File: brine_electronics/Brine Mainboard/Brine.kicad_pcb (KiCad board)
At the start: 2 copper layers, 30.4 x 42.6 mm, 29 parts, among them J1 BATT, J2 BATT_CRG_GND, J3 BATT_CRG_BATT, J4 BATT_CRG_BATT, J5 BATT_CRG_GND, Q1 AO3407A, U1 XIAO-ESP32-S3-SMD, U2 VL53L1CXV0FY1, U3 LTC2954, U4 74AHCT1G125

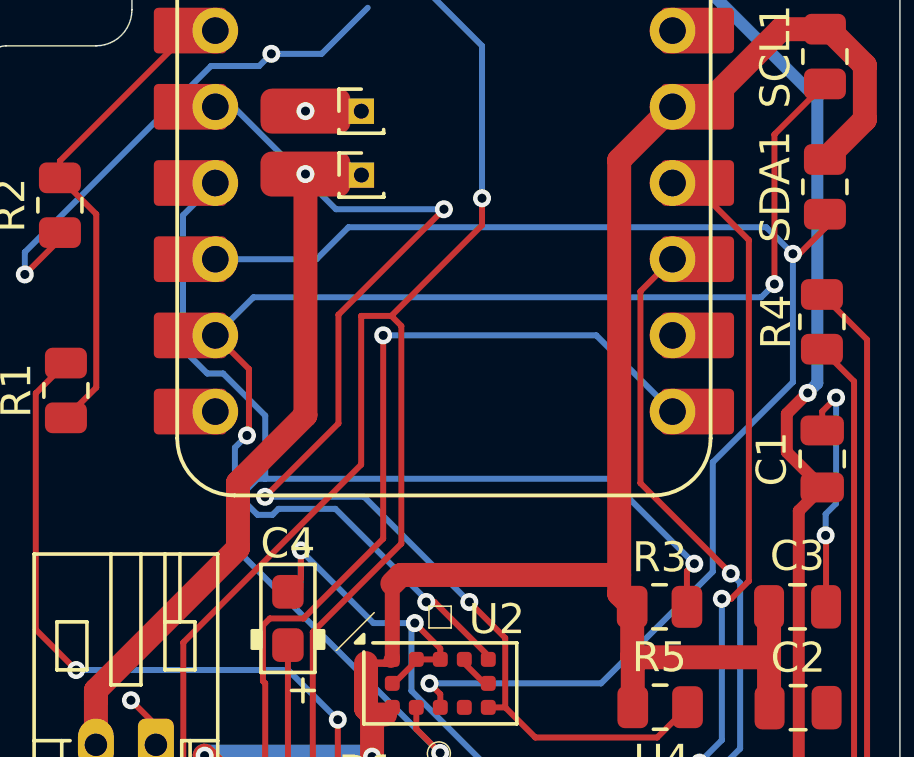
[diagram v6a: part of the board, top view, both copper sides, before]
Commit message: Updated GPIO button wiring ⚡
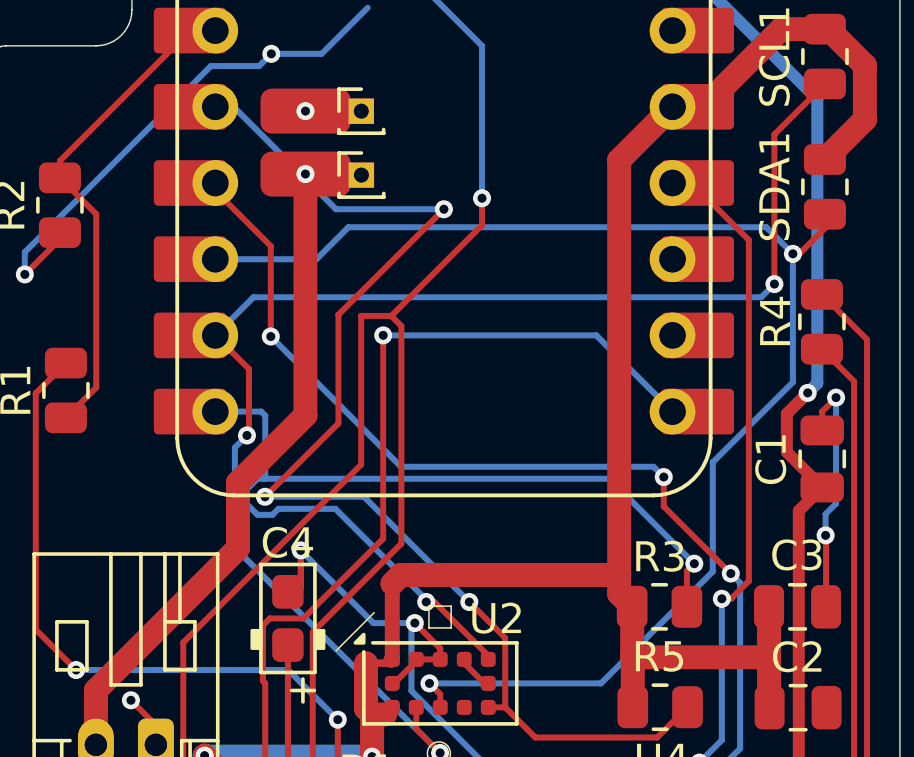
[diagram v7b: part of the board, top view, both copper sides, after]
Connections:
- U1 pad 10: /Button/BUTTON -> unconnected-(U1-GPIO9_D9_MISO-Pad10)
- U1 pad 4: /Distance Sensor/XSHUT -> /Button/BUTTON
- U1 pad 7: unconnected-(U1-GPIO21_D6_TX-Pad7)_1 -> /Distance Sensor/XSHUT
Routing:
- net /Button/BUTTON: track 60.5 -> 73.4 mm, vias 3 -> 5
- net /Distance Sensor/XSHUT: track 41.3 -> 32.6 mm
- net unconnected-(U1-GPIO9_D9_MISO-Pad10): track 0.00 -> 0.83 mm
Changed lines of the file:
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@@
 			(layers "F.Cu" "F.Mask")
 			(roundrect_rratio 0.1)
-			(net "/Distance Sensor/XSHUT")
+			(net "/Button/BUTTON")
 			(pinfunction "GPIO5_A3_D3_4")
 			(pintype "passive")
@@
 			(layers "*.Cu" "*.Mask")
 			(remove_unused_layers no)
-			(net "/Distance Sensor/XSHUT")
+			(net "/Button/BUTTON")
 			(pinfunction "GPIO5_A3_D3_4")
 			(pintype "passive")
@@
 			(layers "F.Cu" "F.Mask")
 			(roundrect_rratio 0.1)
-			(net "unconnected-(U1-GPIO21_D6_TX-Pad7)")
+			(net "/Distance Sensor/XSHUT")
 			(pinfunction "GPIO21_D6_TX_7")
-			(pintype "passive+no_connect")
+			(pintype "passive")
 			(thermal_bridge_angle 45)
 		)
@@
 			(layers "*.Cu" "*.Mask")
 			(remove_unused_layers no)
-			(net "unconnected-(U1-GPIO21_D6_TX-Pad7)_1")
+			(net "/Distance Sensor/XSHUT")
 			(pinfunction "GPIO21_D6_TX_7")
-			(pintype "passive+no_connect")
+			(pintype "passive")
 		)
 		(pad "8" thru_hole circle
@@
 			(layers "*.Cu" "*.Mask")
 			(remove_unused_layers no)
-			(net "/Button/BUTTON")
+			(net "unconnected-(U1-GPIO9_D9_MISO-Pad10)")
 			(pinfunction "GPIO9_D9_MISO_10")
 			(pintype "passive")
@@
 			(layers "F.Cu" "F.Mask")
 			(roundrect_rratio 0.1)
-			(net "/Button/BUTTON")
+			(net "unconnected-(U1-GPIO9_D9_MISO-Pad10)")
 			(pinfunction "GPIO9_D9_MISO_10")
 			(pintype "passive")
@@
 		(net "/Distance Sensor/XSHUT")
 	)
-	(segment
-		(start 143.945 80.772)
-		(end 144.78 80.772)
-		(width 0.2)
-		(layer "F.Cu")
-		(net "/Distance Sensor/XSHUT")
-	)
 	(via
 		(at 160.7462 93.4626)
@@
 	)
 	(segment
-		(start 143.7025 81.8495)
-		(end 144.78 80.772)
-		(width 0.2)
-		(layer "B.Cu")
-		(net "/Distance Sensor/XSHUT")
-	)
-	(segment
 		(start 151.810483 94.660483)
 		(end 148.7831 91.6331)
@@
 	)
 	(segment
-		(start 145.0403 87.122)
-		(end 144.5118 87.122)
-		(width 0.2)
-		(layer "B.Cu")
-		(net "/Distance Sensor/XSHUT")
-	)
-	(segment
 		(start 148.7831 91.6331)
 		(end 146.885543 91.6331)
@@
 	)
 	(segment
-		(start 146.4443 88.526)
-		(end 145.0403 87.122)
-		(width 0.2)
-		(layer "B.Cu")
-		(net "/Distance Sensor/XSHUT")
-	)
-	(segment
 		(start 145.8356 91.481043)
 		(end 145.8356 90.983157)
@@
 	)
 	(segment
-		(start 143.7025 86.3127)
-		(end 143.7025 81.8495)
-		(width 0.2)
-		(layer "B.Cu")
-		(net "/Distance Sensor/XSHUT")
-	)
-	(segment
 		(start 157.914 90.6304)
 		(end 146.4443 90.6304)
@@
 	)
 	(segment
-		(start 144.5118 87.122)
-		(end 143.7025 86.3127)
+		(start 146.4443 88.526)
+		(end 146.3103 88.392)
+		(width 0.2)
+		(layer "B.Cu")
+		(net "/Distance Sensor/XSHUT")
+	)
+	(segment
+		(start 146.3103 88.392)
+		(end 144.78 88.392)
 		(width 0.2)
 		(layer "B.Cu")
@@
 	)
 	(segment
-		(start 142.8457 108.375)
-		(end 142.8457 107.5002)
+		(start 146.629592 85.889198)
+		(end 146.629592 82.875592)
 		(width 0.2)
 		(layer "F.Cu")
@@
 	)
 	(segment
-		(start 160.02 83.312)
-		(end 160.855 83.312)
+		(start 142.8457 108.375)
+		(end 142.8457 107.5002)
 		(width 0.2)
 		(layer "F.Cu")
@@
 	)
 	(segment
-		(start 158.95 84.382)
-		(end 158.95 90.7768)
+		(start 157.2148 108.3602)
+		(end 155.4 110.175)
 		(width 0.2)
 		(layer "F.Cu")
@@
 	)
 	(segment
-		(start 157.2148 108.3602)
-		(end 155.4 110.175)
+		(start 143.945 80.772)
+		(end 144.78 80.772)
 		(width 0.2)
 		(layer "F.Cu")
@@
 	)
 	(segment
-		(start 158.95 90.7768)
-		(end 161.963 93.7898)
+		(start 161.963 93.7898)
+		(end 159.727867 91.554667)
 		(width 0.2)
 		(layer "F.Cu")
@@
 	)
 	(segment
+		(start 159.727867 91.554667)
+		(end 159.727867 90.572667)
+		(width 0.2)
+		(layer "F.Cu")
+		(net "/Button/BUTTON")
+	)
+	(segment
 		(start 143.757 108.375)
 		(end 142.8457 108.375)
@@
 	)
 	(segment
-		(start 160.02 83.312)
-		(end 158.95 84.382)
+		(start 146.629592 82.875592)
+		(end 144.78 81.026)
 		(width 0.2)
 		(layer "F.Cu")
@@
 		(net "/Button/BUTTON")
 	)
+	(segment
+		(start 144.78 81.026)
+		(end 144.78 80.772)
+		(width 0.2)
+		(layer "F.Cu")
+		(net "/Button/BUTTON")
+	)
 	(via
 		(at 141.998 106.6525)
@@
 	)
 	(via
+		(at 159.727867 90.572667)
+		(size 0.6)
+		(drill 0.3)
+		(layers "F.Cu" "B.Cu")
+		(net "/Button/BUTTON")
+	)
+	(via
 		(at 161.963 93.7898)
 		(size 0.6)
@@
 		(net "/Button/BUTTON")
 	)
+	(via micro
+		(at 146.629592 85.889198)
+		(size 0.6)
+		(drill 0.3)
+		(layers "F.Cu" "B.Cu")
+		(net "/Button/BUTTON")
+	)
 	(via
 		(at 157.2148 101.5198)
@@
 	)
 	(segment
+		(start 150.970794 90.2304)
+		(end 146.629592 85.889198)
+		(width 0.2)
+		(layer "B.Cu")
+		(net "/Button/BUTTON")
+	)
+	(segment
 		(start 160.378 101.5198)
 		(end 157.2148 101.5198)
@@
 	)
 	(segment
+		(start 159.727867 90.572667)
+		(end 159.3856 90.2304)
+		(width 0.2)
+		(layer "B.Cu")
+		(net "/Button/BUTTON")
+	)
+	(segment
+		(start 159.3856 90.2304)
+		(end 150.970794 90.2304)
+		(width 0.2)
+		(layer "B.Cu")
+		(net "/Button/BUTTON")
+	)
+	(segment
 		(start 141.998 106.6525)
 		(end 152.0821 106.6525)
@@
 		(net "Net-(D2-DIN)")
 	)
+	(segment
+		(start 160.02 83.312)
+		(end 160.855 83.312)
+		(width 0.2)
+		(layer "F.Cu")
+		(net "unconnected-(U1-GPIO9_D9_MISO-Pad10)")
+	)
 	(zone

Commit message: Updated distance sensor routing 📏
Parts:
- U2: footprint Sensor_Distance:ST_VL53L1x -> VL53L1CXV0FY_1:VL53L1CXV0FY1
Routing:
- net +3.3V: track 66.1 -> 67.8 mm
